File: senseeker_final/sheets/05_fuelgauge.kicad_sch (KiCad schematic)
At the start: 2 parts, among them P2 Header-Male-2.54_2x2, U1 MAX17048G+T10

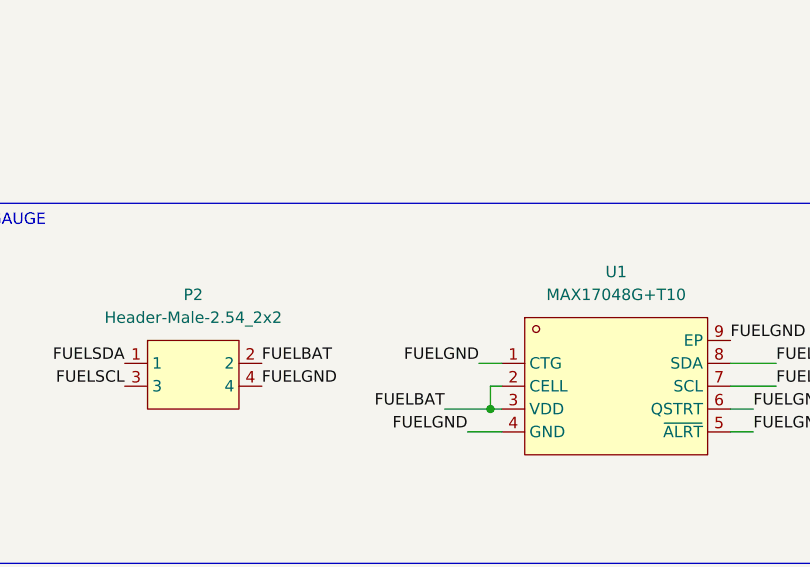
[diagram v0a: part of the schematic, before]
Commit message: formatting changes for LM2596, now ready to branch of off and make our seperate PCB and then compare
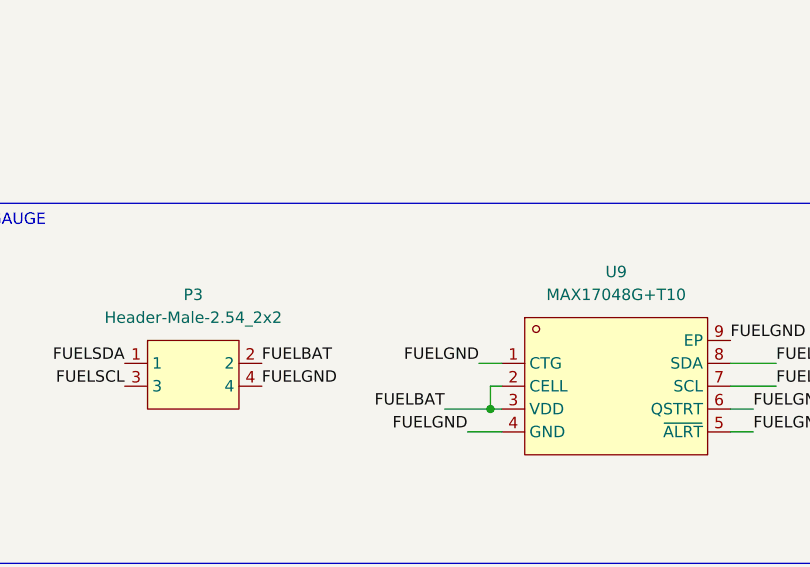
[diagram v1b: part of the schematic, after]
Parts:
- renumbered P2 to P3, U1 to U9
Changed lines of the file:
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@@
 		(dnp no)
 		(fields_autoplaced yes)
-		(property "Reference" "U1"
+		(property "Reference" "U9"
 			(at 158.75 71.12 0)
 			(effects
@@
 			(project "senseeker_final"
 				(path "/529bc8a5-ffae-43ac-972d-caccc3afab85/8c3d0b7d-92b0-403f-802a-8a5a7d9fa34c"
-					(reference "U1")
+					(reference "U9")
 					(unit 1)
 				)
@@
 		(dnp no)
 		(fields_autoplaced yes)
-		(property "Reference" "P2"
+		(property "Reference" "P3"
 			(at 111.76 73.66 0)
 			(effects
@@
 			(project "senseeker_final"
 				(path "/529bc8a5-ffae-43ac-972d-caccc3afab85/8c3d0b7d-92b0-403f-802a-8a5a7d9fa34c"
-					(reference "P2")
+					(reference "P3")
 					(unit 1)
 				)
